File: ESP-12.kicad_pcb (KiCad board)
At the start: 2 copper layers, 30 x 34 mm, 16 parts, among them IC1 REG, P1 GPIO_1, P2 GPIO_2, P3 UART, P4 SPI, P5 P_IN, SW1 RESET, SW2 FLASH, U1 ESP-12E

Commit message: Initial commit
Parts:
- removed IC1: REG, TO_SOT_Packages_SMD:SOT-223
- removed P4: SPI, Pin_Headers:Pin_Header_Straight_1x06
- removed P5: P_IN, Pin_Headers:Pin_Header_Straight_1x02
- added R6: R, Resistors_SMD:R_0805_HandSoldering, B.Cu at (27.7, 24.1)
- added R7: R, Resistors_SMD:R_0805_HandSoldering, B.Cu at (50.5, 24.1)
- P3: value UART -> SPI; footprint Pin_Headers:Pin_Header_Straight_1x04 -> Pin_Headers:Pin_Header_Straight_1x06
- SW1, SW2: moved to F.Cu
- moved SW1 165.2 mm to (27.6, 24.1), turned to 270 degrees
- moved R1 161.0 mm to (34.8, 28.8), turned to 0 degrees
- moved R2 157.7 mm to (34.8, 31.0), turned to 0 degrees
- moved C2 156.6 mm to (34.8, 41.0)
- moved C3 156.6 mm to (34.8, 38.8)
- moved R3 156.6 mm to (42.8, 36.5)
- moved R4 156.6 mm to (42.8, 38.8)
- moved R5 156.6 mm to (42.8, 41.0)
- moved U1 156.4 mm to (31.0, 28.8)
- moved P2 156.2 mm to (51.8, 30.2)
- moved P1 156.1 mm to (26.4, 30.3)
- moved SW2 153.3 mm to (50.5, 24.2), turned to 90 degrees
- moved P3 149.2 mm to (44.2, 48.1), turned to 270 degrees
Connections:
- P1 pad 1: /ADC -> /RST
- P1 pad 2: /GPIO16 -> /ADC
- P1 pad 3: /GPIO14 -> /CH_PD
- P1 pad 4: /GPIO13 -> /GPIO16
- P1 pad 5: /GPIO12 -> /GPIO14
- P1 pad 6: /GPIO9 -> /GPIO12
- P1 pad 7: VCC -> /GPIO13
- P1 pad 8: GND -> VCC
- R1 pad 1: Net-(R1-Pad1) -> /RST
- R2 pad 1: Net-(R2-Pad1) -> /CH_PD
- SW1 pad 1: Net-(R1-Pad1) -> /RST
- SW1 pad 2: GND -> Net-(R6-Pad2)
- SW2 pad 2: GND -> Net-(R7-Pad2)
- U1 pad 1: Net-(R1-Pad1) -> /RST
- U1 pad 3: Net-(R2-Pad1) -> /CH_PD
- U1 pad 6: /GPIO13 -> /GPIO12
- U1 pad 7: /GPIO12 -> /GPIO13
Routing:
- net VCC: track 95.2 -> 34.4 mm, vias 3 -> 0
- net /GPIO0: track 12.1 -> 23.2 mm
- net Net-(R1-Pad1): track 10.5 -> 0.00 mm
- net /GPIO9: track 14.8 -> 4.89 mm
- net /RST: track 0.00 -> 9.59 mm
- net /GPIO10: track 13.9 -> 4.67 mm
- net /CH_PD: track 0.00 -> 9.24 mm
- net /GPIO15: track 6.81 -> 11.7 mm
- net /Vin: track 4.26 -> 0.00 mm
- net Net-(R7-Pad2): track 0.00 -> 3.35 mm, vias 0 -> 1
- net /GPIO2: track 7.77 -> 11.1 mm
- net Net-(R6-Pad2): track 0.00 -> 3.24 mm, vias 0 -> 1
- net Net-(R2-Pad1): track 3.06 -> 0.00 mm
- net /MISO: track 7.63 -> 5.12 mm
- net /GPIO13: track 5.34 -> 7.64 mm
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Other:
- board size 30 x 34 mm -> 29 x 30 mm
- board text added: "ESPBoardv1.0"
- board text added: "www.falseascension.xyz"

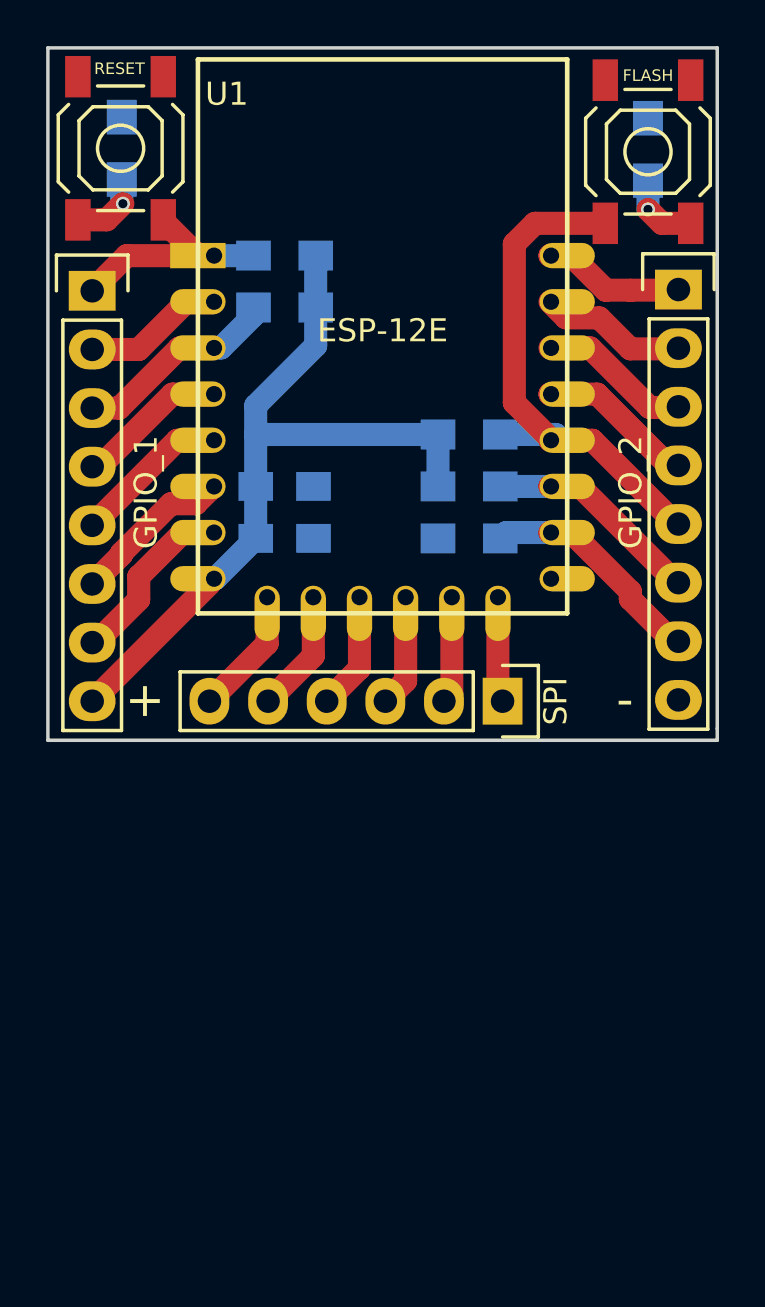
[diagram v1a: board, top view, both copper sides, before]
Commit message: Regulator, LED, decreased width, + more
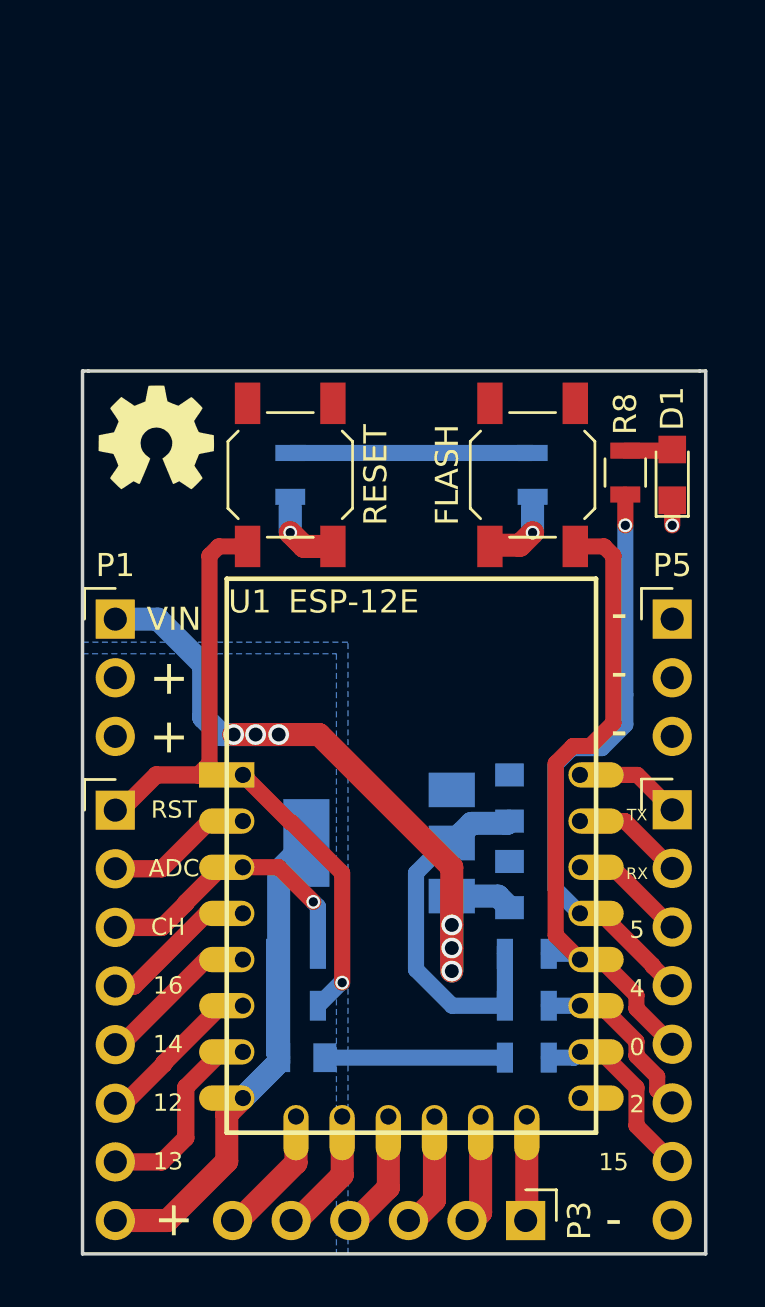
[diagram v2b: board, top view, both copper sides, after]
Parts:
- removed the P2 at (51.8, 30.2)
- added C1: 10uF, Capacitors_SMD:C_0805, B.Cu at (44.5, 56.0)
- added D1: , LEDs:LED_0805, F.Cu at (51.5, 38.2)
- added G***: OSHW_silkscreen-back_3mm, Misc_Footprints:FalseAscension_TextOnly, B.Cu at (51.0, 35.8)
- added G***: OSHW_silkscreen-front_6mm, OSHW:OSHW_silkscreen-front_5mm, F.Cu at (29.2, 36.6)
- added P1: VCC, Misc_Footprints:Pin_Header_Straight_1x03_Pitch2.54mm, F.Cu at (27.4, 44.5)
- added P4: GPIO_2, Misc_Footprints:Pin_Header_Straight_1x08_Pitch2.54mm, F.Cu at (51.5, 52.8)
- added P5: GND, Misc_Footprints:Pin_Header_Straight_1x03_Pitch2.54mm, F.Cu at (51.5, 44.5)
- added R8: , Resistors_SMD:R_0805, F.Cu at (49.5, 38.1)
- added U2: AP1117-33, TO_SOT_Packages_SMD:SOT-223-3Lead_TabPin2, B.Cu at (38.9, 54.2)
- C2: value 100nF -> 10uF; footprint Capacitors_SMD:C_0805_HandSoldering -> Capacitors_SMD:C_0805
- C3: value 10uF -> 100nF; footprint Capacitors_SMD:C_0805_HandSoldering -> Capacitors_SMD:C_0805
- P2: renamed from P1; footprint Pin_Headers:Pin_Header_Straight_1x08 -> Misc_Footprints:Pin_Header_Straight_1x08_Pitch2.54mm
- P3: footprint Pin_Headers:Pin_Header_Straight_1x06 -> Misc_Footprints:Pin_Header_Straight_1x06_Pitch2.54mm
- R1, R2, R3, R4, R5, R6, R7: footprint Resistors_SMD:R_0805_HandSoldering -> Resistors_SMD:R_0805
- SW1: value RESET -> FLASH
- SW2: value FLASH -> RESET
- moved R1 32.5 mm to (35.2, 61.2), turned to 180 degrees
- moved R2 28.0 mm to (35.2, 59.0), turned to 180 degrees
- moved C3 24.8 mm to (35.5, 63.5)
- moved SW1 22.8 mm to (45.5, 38.2)
- moved R3 22.6 mm to (45.2, 59.0)
- moved R4 22.6 mm to (45.2, 61.2)
- moved R5 22.6 mm to (45.2, 63.5)
- moved U1 22.5 mm to (32.2, 51.2)
- moved P2 22.5 mm to (27.4, 52.8)
- moved P3 22.5 mm to (45.2, 70.6)
- moved SW2 20.9 mm to (35.0, 38.2)
- moved R6 15.9 mm to (35.0, 38.2)
- moved R7 15.0 mm to (45.5, 38.2)
- moved C2 14.9 mm to (44.5, 52.2), turned to 90 degrees
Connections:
- SW1 pad 1: /RST -> /GPIO0
- SW1 pad 2: Net-(R6-Pad2) -> Net-(R7-Pad2)
- SW2 pad 1: /GPIO0 -> /RST
- SW2 pad 2: Net-(R7-Pad2) -> Net-(R6-Pad2)
- U1 pad 10: /MISO -> /GPIO15
- U1 pad 11: /GPIO9 -> /GPIO2
- U1 pad 12: /GPIO10 -> /GPIO0
- U1 pad 13: /MOSI -> /GPIO4
- U1 pad 14: /SCLK -> /GPIO5
- U1 pad 15: GND -> /RXD
- U1 pad 16: /GPIO15 -> /TXD
- U1 pad 17: /GPIO2 -> /SS
- U1 pad 18: /GPIO0 -> /MISO
- U1 pad 19: /GPIO4 -> /GPIO9
- U1 pad 20: /GPIO5 -> /GPIO10
- U1 pad 21: /RXD -> /MOSI
- U1 pad 22: /TXD -> /SCLK
- U1 pad 9: /SS -> GND
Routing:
- net /VIN: track 0.00 -> 33.0 mm, vias 0 -> 6
- net /RST: track 9.59 -> 29.7 mm, vias 0 -> 1
- net GND: track 0.76 -> 19.6 mm, vias 0 -> 1
- net /GPIO4: track 7.79 -> 25.9 mm, vias 0 -> 1
- net VCC: track 34.4 -> 44.1 mm
- net /GPIO0: track 23.2 -> 28.5 mm
- net /GPIO2: track 11.1 -> 7.80 mm
- net /GPIO15: track 11.7 -> 8.39 mm
- net /CH_PD: track 9.24 -> 12.4 mm, vias 0 -> 1
- net /TXD: track 7.12 -> 4.63 mm
- net Net-(D1-Pad2): track 0.00 -> 2.05 mm
- net /RXD: track 6.34 -> 4.85 mm
- net /GPIO5: track 6.56 -> 5.07 mm
- net /GPIO13: track 7.64 -> 8.54 mm
- added copper zone on B.Cu, net VCC
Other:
- board size 29 x 30 mm -> 27 x 38.2 mm
- board text added: "0"
- board text added: "12"
- board text added: "13"
- board text added: "14"
- board text added: "15"
- board text added: "16"
- board text added: "2"
- board text added: "4"
- board text added: "5"
- board text added: "ADC"
- board text added: "CH"
- board text added: "RST"
- board text added: "RX"
- board text added: "TX"
- board text added: "VIN"
- board text removed: "ESPBoardv1.0"
- board text removed: "www.falseascension.xyz"
